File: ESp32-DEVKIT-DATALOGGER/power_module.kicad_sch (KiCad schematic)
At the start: 15 parts, among them J501 7.62mm 2-Pin Screw Terminal, J502 Barrel_Jack_Switch_Pin3Ring, U501 AMS1117-3.3

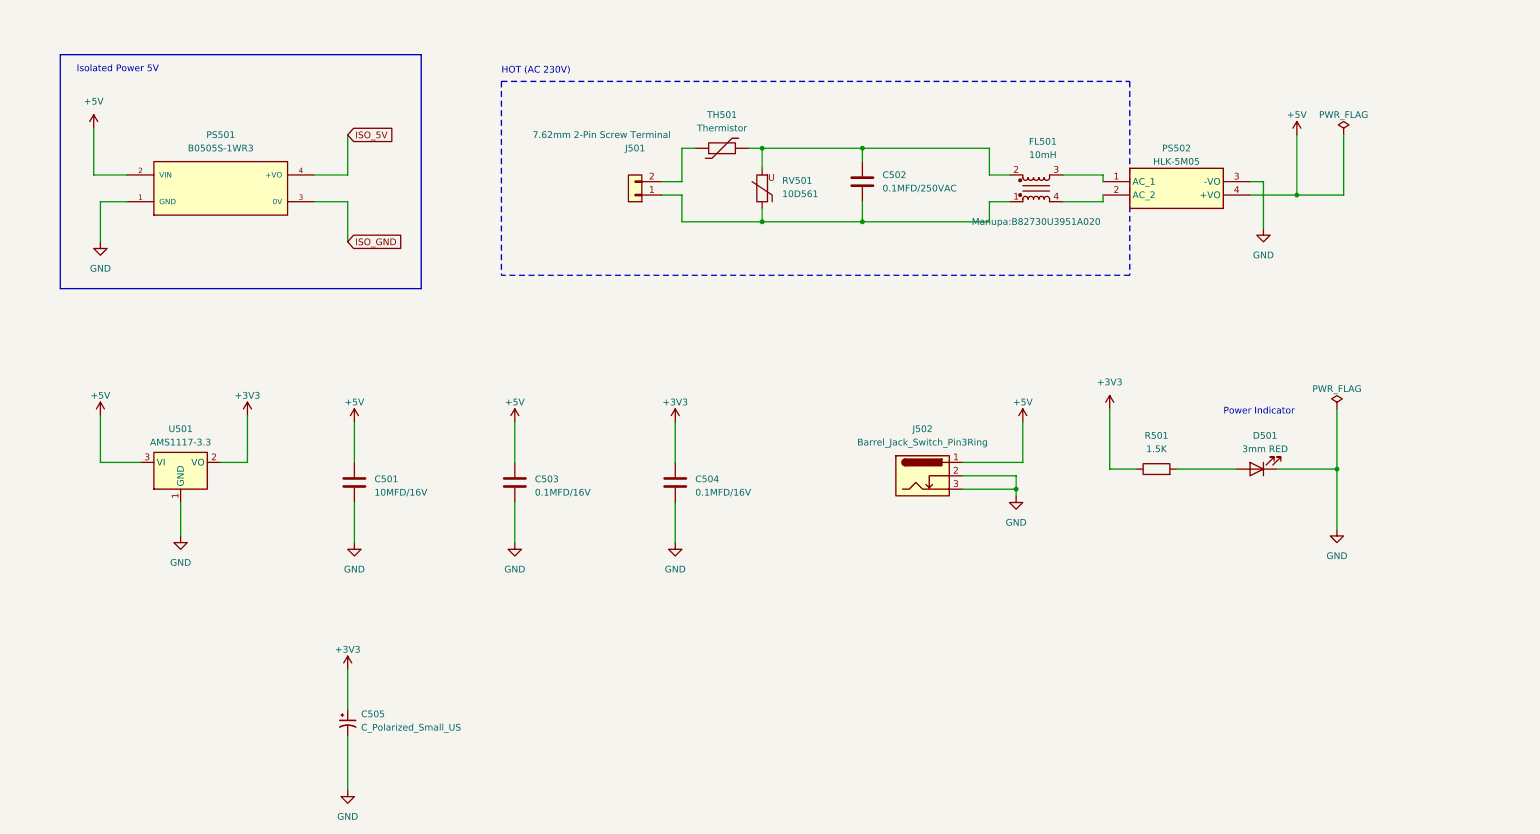
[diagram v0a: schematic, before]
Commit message: Small Changes
Adding I2C components
More RS485
And it is required changing the  Labels for RS485 . for 3 different channels
And Make them ISO Pins
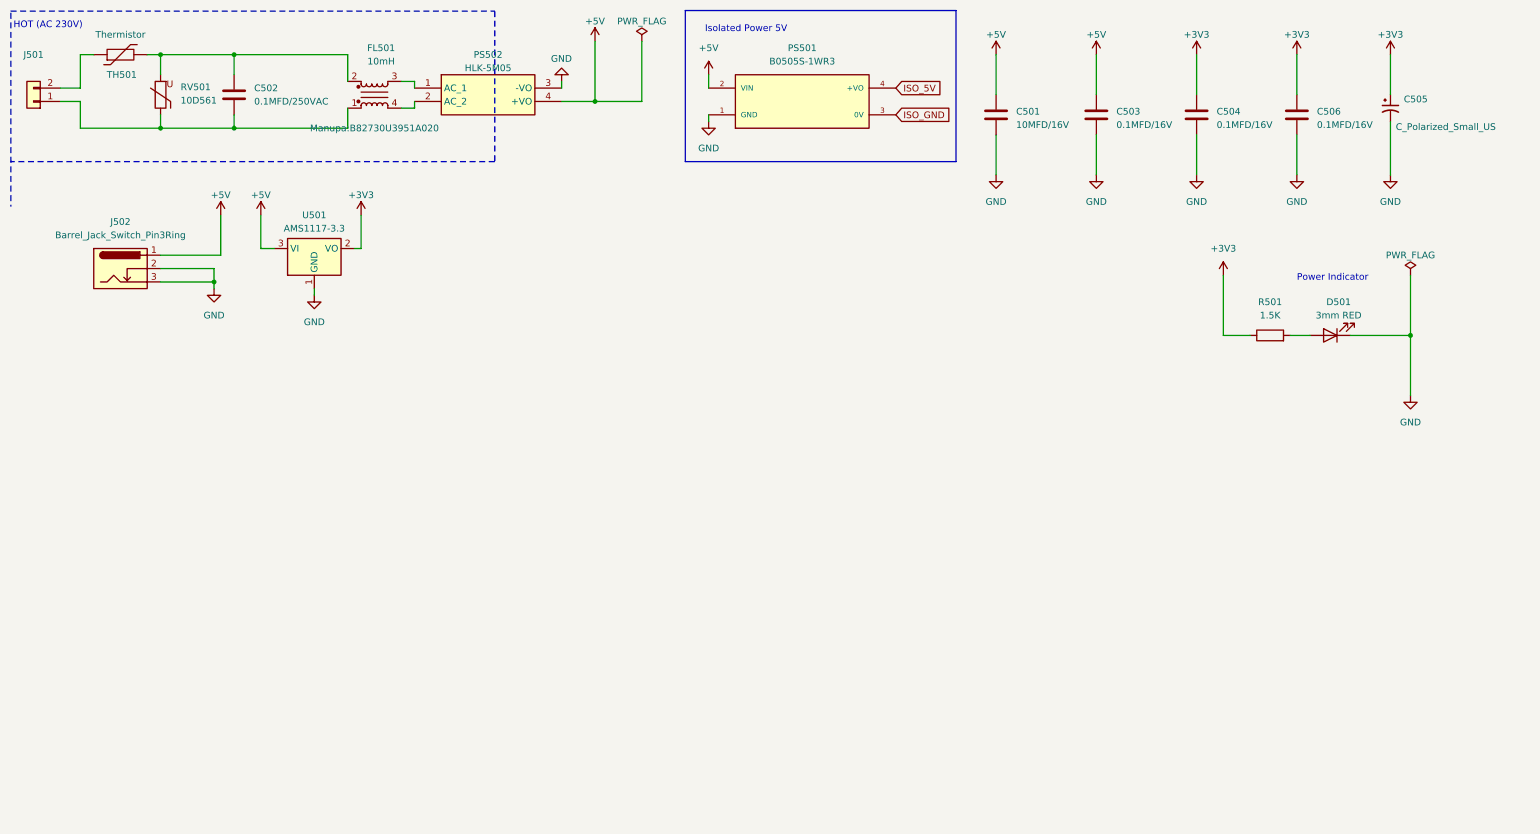
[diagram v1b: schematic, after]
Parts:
- added C506: 0.1MFD/16V, Capacitor_SMD:C_0805_2012Metric_Pad1.18x1.45mm_HandSolder, symbol Device:C
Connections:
- net +3V3: now also C506.1
- net GND: now also C506.2
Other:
- moved on the sheet: C501, C502, C503, C504, C505, D501, FL501, J501, J502, PS501, PS502, R501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
